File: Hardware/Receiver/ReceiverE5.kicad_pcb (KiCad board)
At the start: 4 copper layers, 50 x 30 mm, 43 parts, among them J1 KBUS, J2 AVR-PDI-6A, J3 CONN_01X08, J4 CONN_01X06, J5 CONN_01X06, J6 CONN_01X04, J7 CONN_01X04, U1 ATXMEGA32E5-A, U2 LM2731, U3 SN74LV07A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

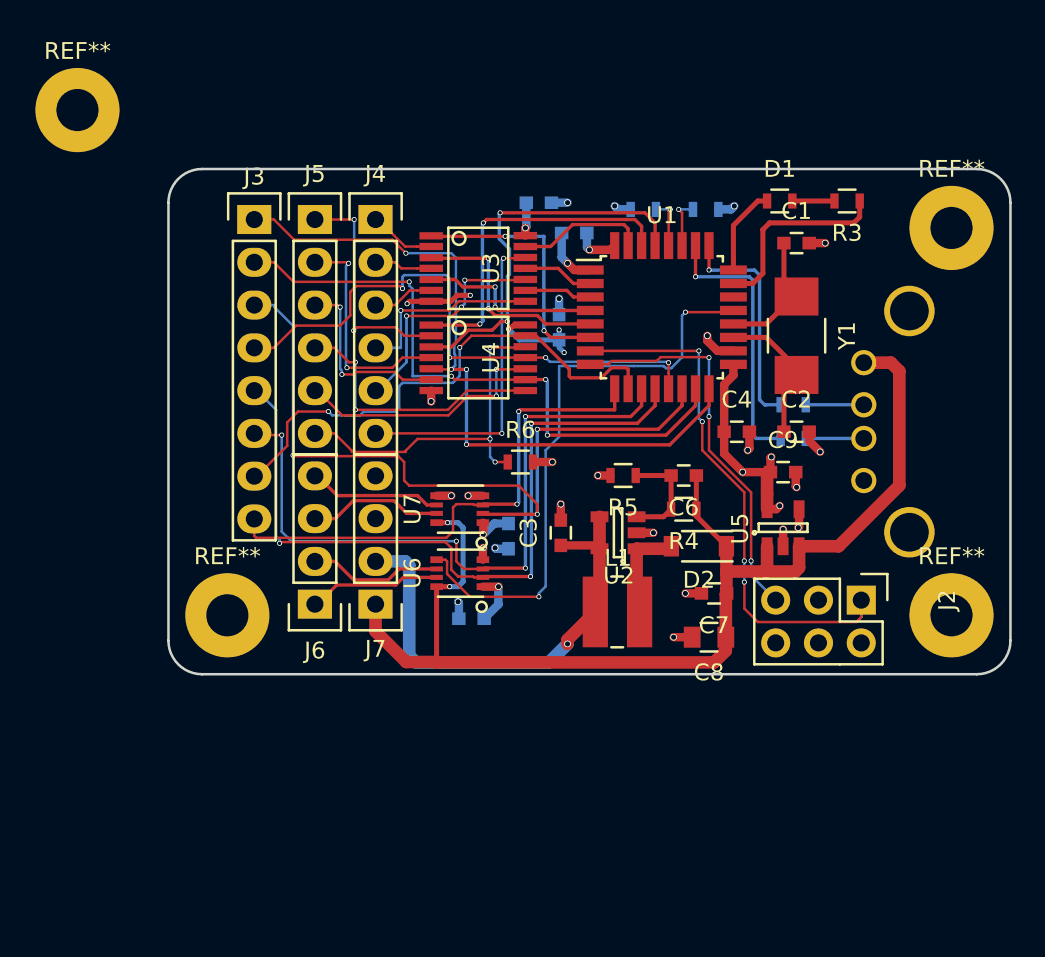
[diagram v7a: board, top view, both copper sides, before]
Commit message: Changed all holes to min 3mm, need to fix DRC errors
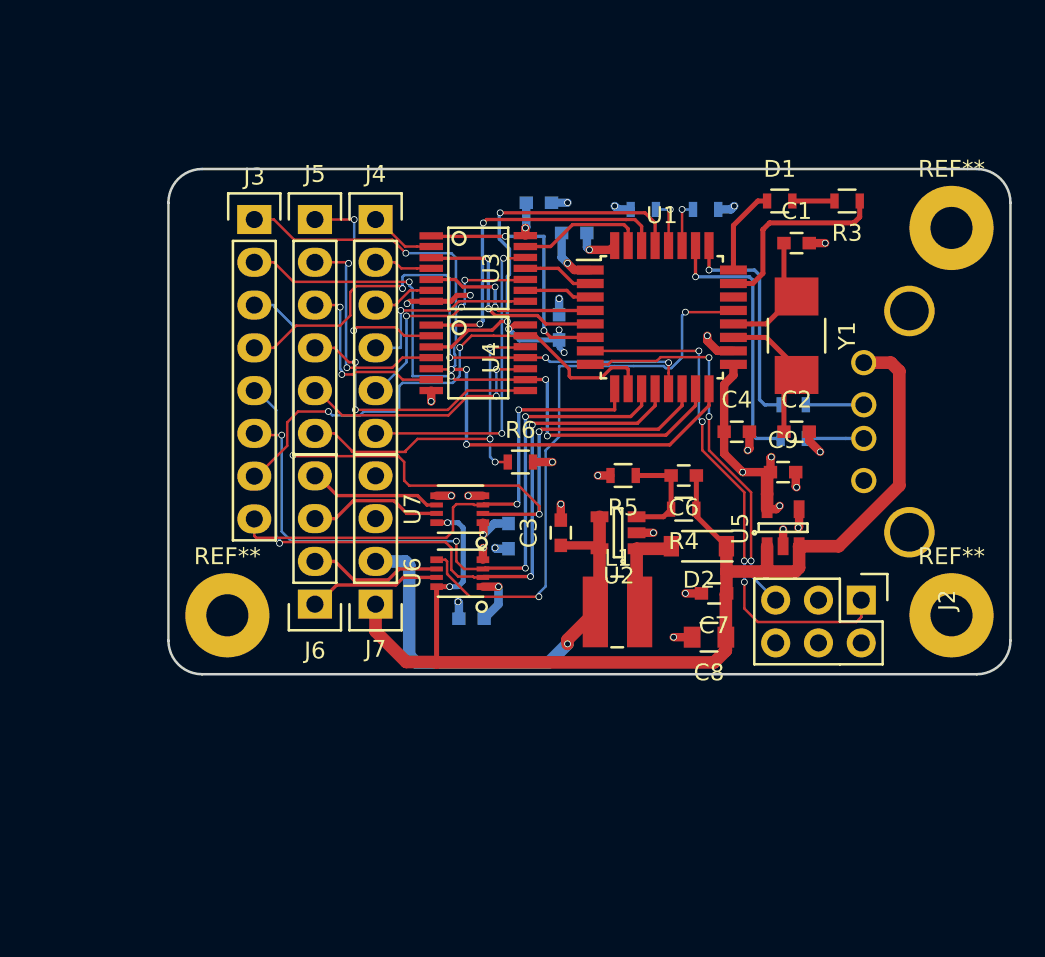
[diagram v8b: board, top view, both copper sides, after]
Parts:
- removed the REF** at (61.6, 59.5)
